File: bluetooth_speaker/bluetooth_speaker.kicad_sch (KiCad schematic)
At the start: 19 parts, among them J1 Conn_Coaxial, J2 USB_C_Receptacle_USB2.0_16P, J3 282836-4, U4 ESP32-D0WD-V3, Y1 40MHz(±10 ppm)

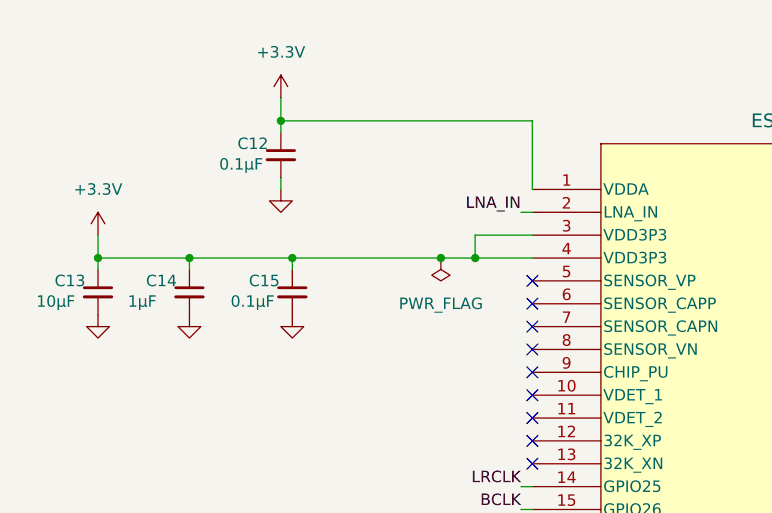
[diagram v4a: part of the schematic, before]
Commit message: Added missing inductor
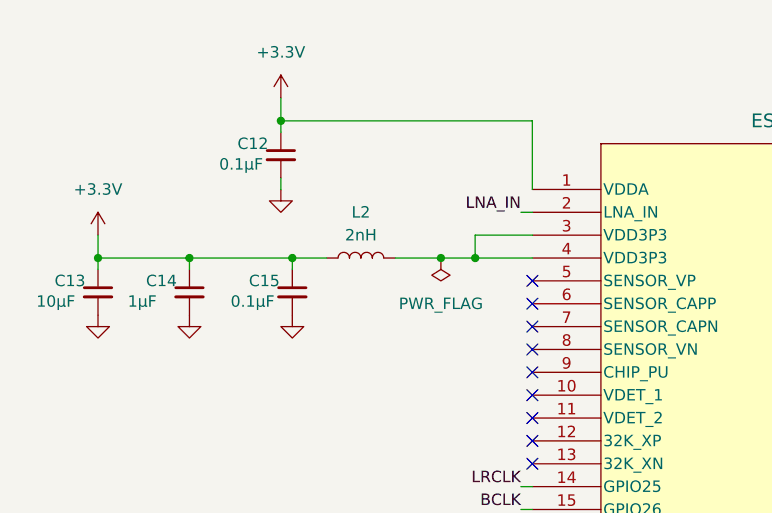
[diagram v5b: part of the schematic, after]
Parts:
- added L2: 2nH, SamacSys_Parts:MHQ1005, symbol Device:L
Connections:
- net +3.3V: now also L2.1; no longer U4.3 (VDD3P3), U4.4 (VDD3P3)
- new net: L2.2, U4.3 (VDD3P3), U4.4 (VDD3P3)
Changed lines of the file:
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@@
 	)
 	(junction
+		(at 43.18 39.37)
+		(diameter 0)
+		(color 0 0 0 0)
+	)
+	(junction
 		(at 63.5 39.37)
 		(diameter 0)
@@
 	)
 	(junction
+		(at 59.69 39.37)
+		(diameter 0)
+		(color 0 0 0 0)
+	)
+	(junction
 		(at 160.02 39.37)
 		(diameter 0)
@@
 	)
 	(junction
-		(at 59.69 39.37)
-		(diameter 0)
-		(color 0 0 0 0)
-	)
-	(junction
 		(at 168.91 127)
 		(diameter 0)
@@
 	)
 	(junction
-		(at 43.18 39.37)
-		(diameter 0)
-		(color 0 0 0 0)
-	)
-	(junction
 		(at 21.59 39.37)
 		(diameter 0)
@@
 	(wire
 		(pts
+			(xy 54.61 39.37) (xy 59.69 39.37)
+		)
+		(stroke
+			(width 0)
+			(type default)
+		)
+	)
+	(wire
+		(pts
 			(xy 236.22 133.35) (xy 242.57 133.35)
 		)
@@
 	(wire
 		(pts
+			(xy 43.18 39.37) (xy 46.99 39.37)
+		)
+		(stroke
+			(width 0)
+			(type default)
+		)
+	)
+	(wire
+		(pts
 			(xy 232.41 73.66) (xy 237.49 73.66)
 		)
@@
 	(wire
 		(pts
-			(xy 43.18 39.37) (xy 59.69 39.37)
-		)
-		(stroke
-			(width 0)
-			(type default)
-		)
-	)
-	(wire
-		(pts
 			(xy 21.59 39.37) (xy 31.75 39.37)
 		)
@@
 			)
 		)
-		(property "Datasheet" "~"
+		(property "Datasheet" "https://www.mouser.pl/ProductDetail/Taoglas/EMPCB.SMAFSTJ.C.HT?qs=AL7xPqYNrmS49k5WLHoXWA%3D%3D"
 			(at 250.19 133.35 0)
 			(effects
@@
 					(unit 1)
 				)
+			)
+		)
+	)
+	(symbol
+		(lib_id "Device:L")
+		(at 50.8 39.37 90)
+		(unit 1)
+		(exclude_from_sim no)
+		(in_bom yes)
+		(on_board yes)
+		(dnp no)
+		(fields_autoplaced yes)
+		(property "Reference" "L2"
+			(at 50.8 34.29 90)
+			(effects
+				(font
+					(size 1.27 1.27)
+				)
+			)
+		)
+		(property "Value" "2nH"
+			(at 50.8 36.83 90)
+			(effects
+				(font
+					(size 1.27 1.27)
+				)
+			)
+		)
+		(property "Footprint" "SamacSys_Parts:MHQ1005"
+			(at 50.8 39.37 0)
+			(effects
+				(font
+					(size 1.27 1.27)
+				)
+				(hide yes)
+			)
+		)
+		(property "Datasheet" "https://www.mouser.pl/ProductDetail/TDK/MHQ1005P2N0BTD25?qs=sGAEpiMZZMv126LJFLh8y5lwrxezZJ61ff3nV176I9k%3D"
+			(at 50.8 39.37 0)
+			(effects
+				(font
+					(size 1.27 1.27)
+				)
+				(hide yes)
+			)
+		)
+		(property "Description" "Inductor"
+			(at 50.8 39.37 0)
+			(effects
+				(font
+					(size 1.27 1.27)
+				)
+				(hide yes)
+			)
+		)
+		(pin "1"
+		)
+		(pin "2"
+		)
+		(instances
+			(project ""
+				(path "/13ff5fb5-140a-4554-92d9-4ae3849ea082"
+					(reference "L2")
+					(unit 1)
+				)

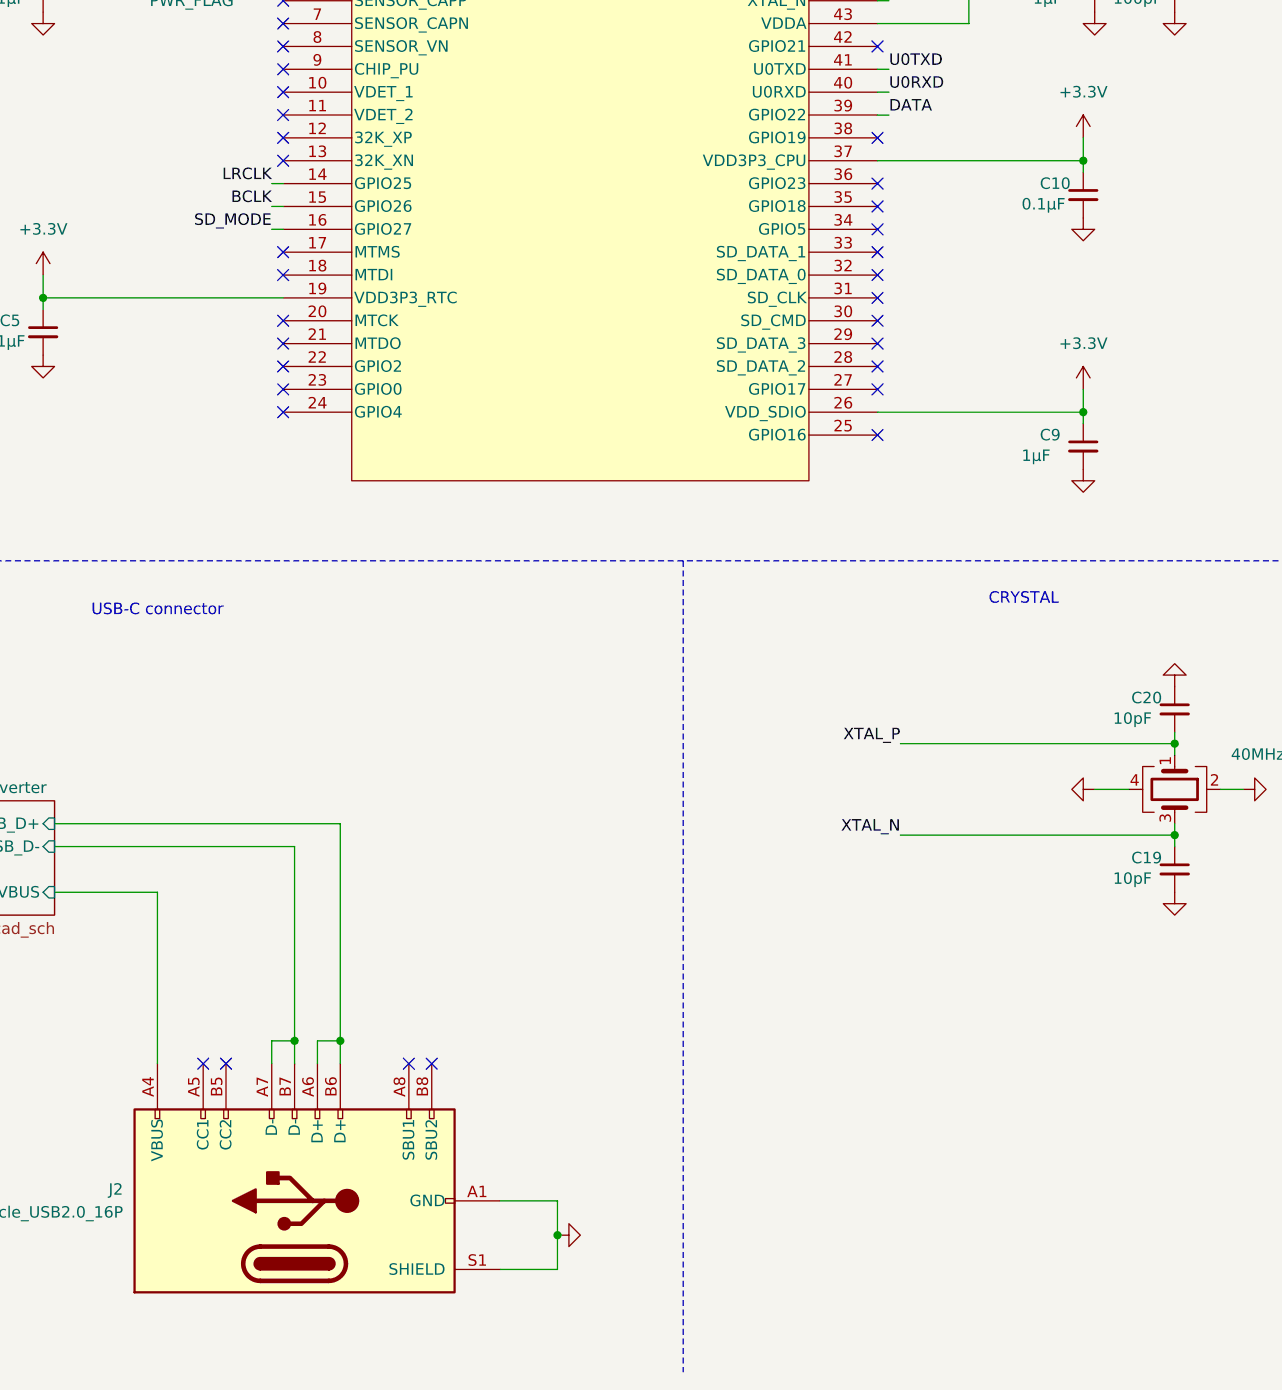
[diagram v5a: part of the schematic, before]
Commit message: Realigned components on PCB
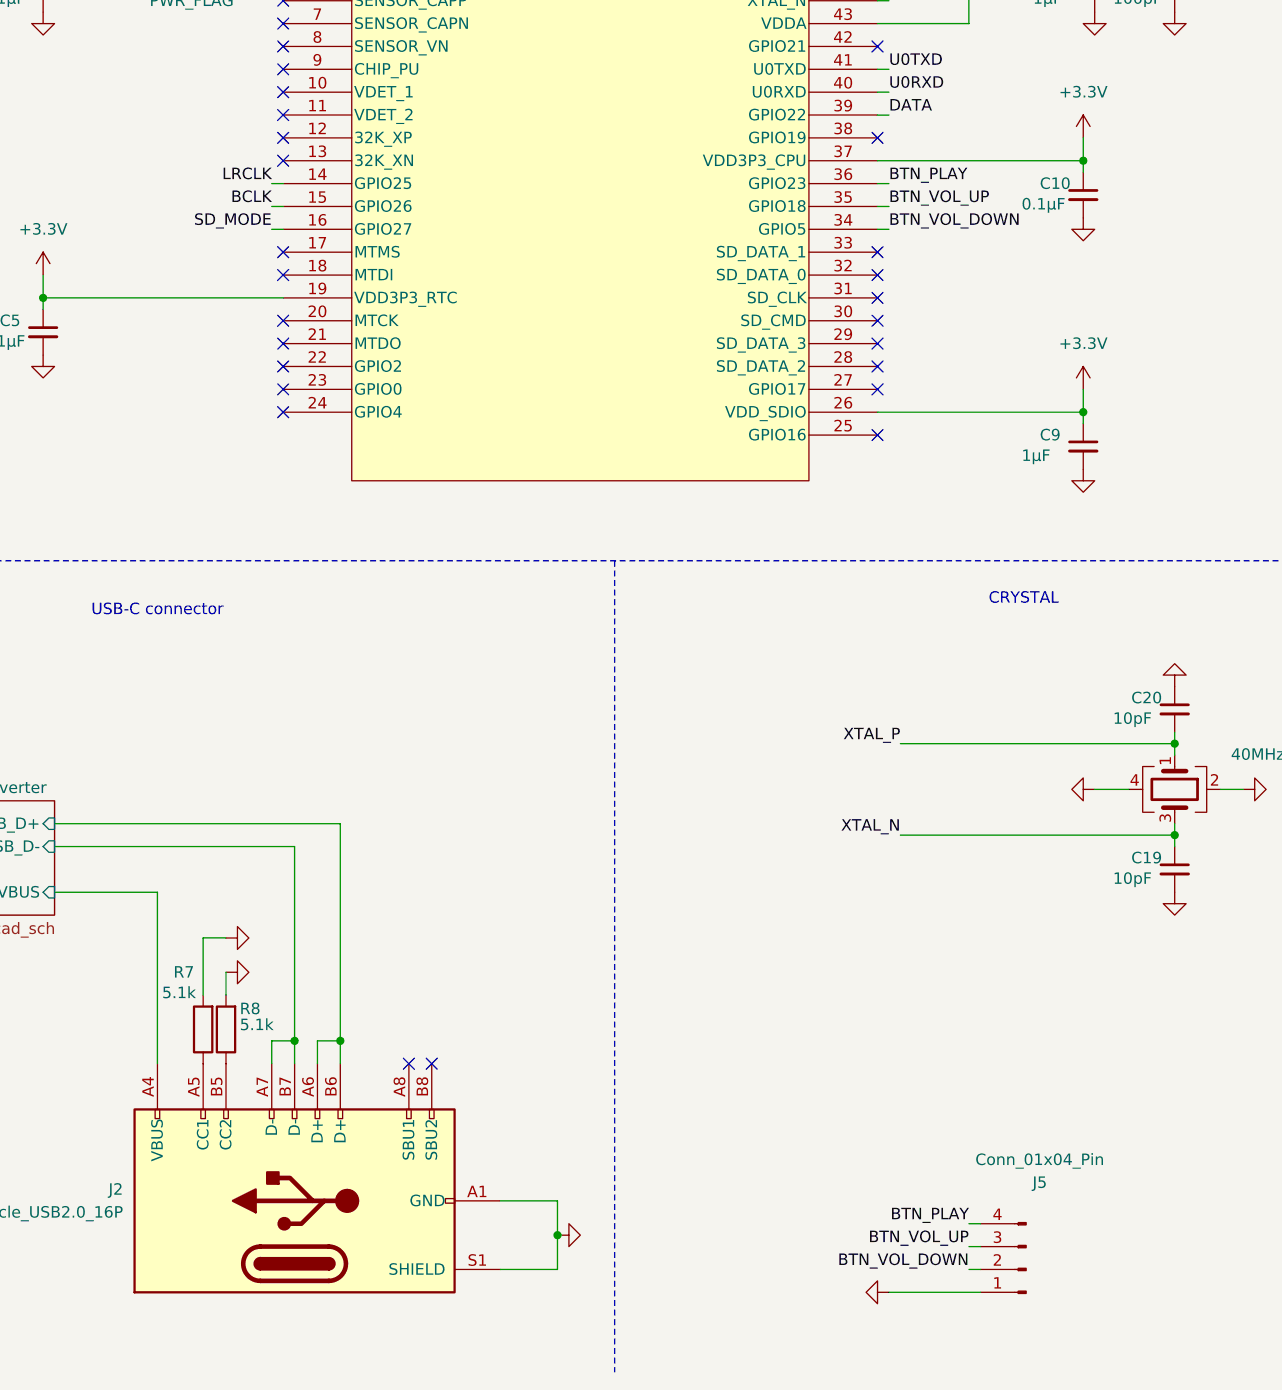
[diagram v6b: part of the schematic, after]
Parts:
- added J5: Conn_01x04_Pin, Connector_JST:JST_PH_B4B-PH-K_1x04_P2.00mm_Vertical, symbol Connector:Conn_01x04_Pin
- added R7, R8: 5.1k, Resistor_SMD:R_0603_1608Metric_Pad0.98x0.95mm_HandSolder, symbol Device:R
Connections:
- net GND: now also J5.1 (Pin_1), R7.2, R8.2
- net at J2.A5 (CC1): now also R7.1
- net at J2.B5 (CC2): now also R8.1
- net BTN_VOL_DOWN: now reaches U4.34 (GPIO5)
- net BTN_VOL_DOWN: now also J5.2 (Pin_2)
- net BTN_VOL_UP: now reaches U4.35 (GPIO18)
- net BTN_VOL_UP: now also J5.3 (Pin_3)
- net BTN_PLAY: now reaches U4.36 (GPIO23)
- net BTN_PLAY: now also J5.4 (Pin_4)
- no-connect marks 35 -> 30

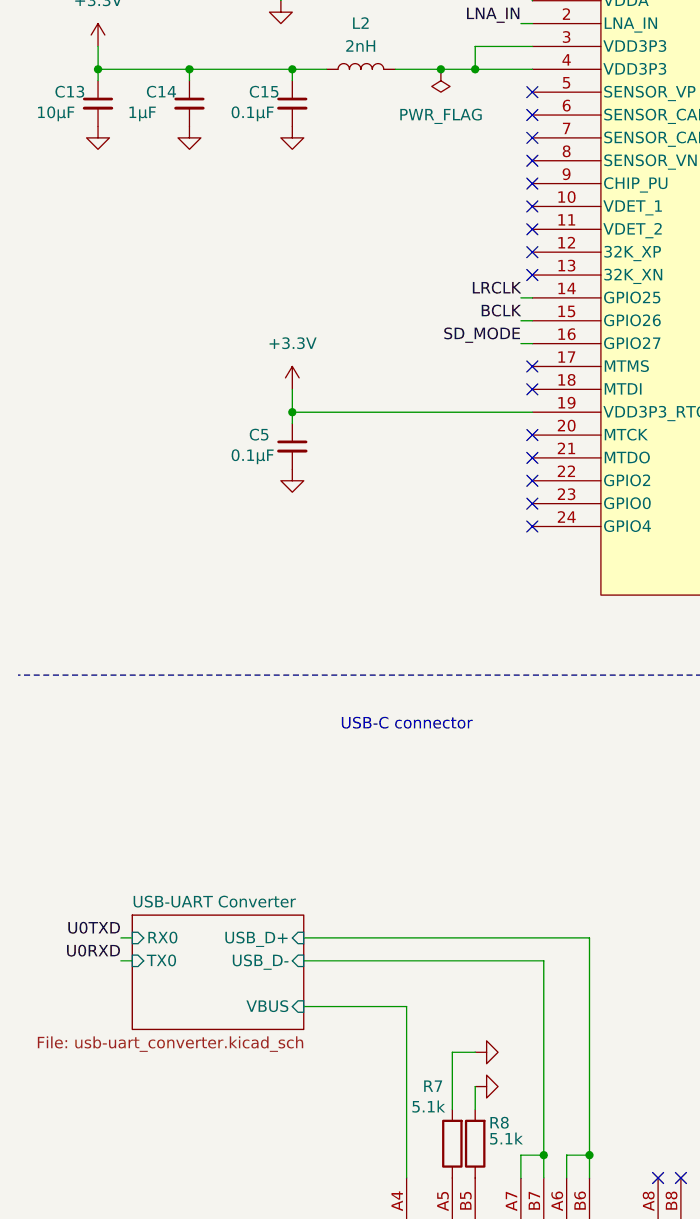
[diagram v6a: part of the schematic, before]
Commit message: Added auto-programming through CP2102
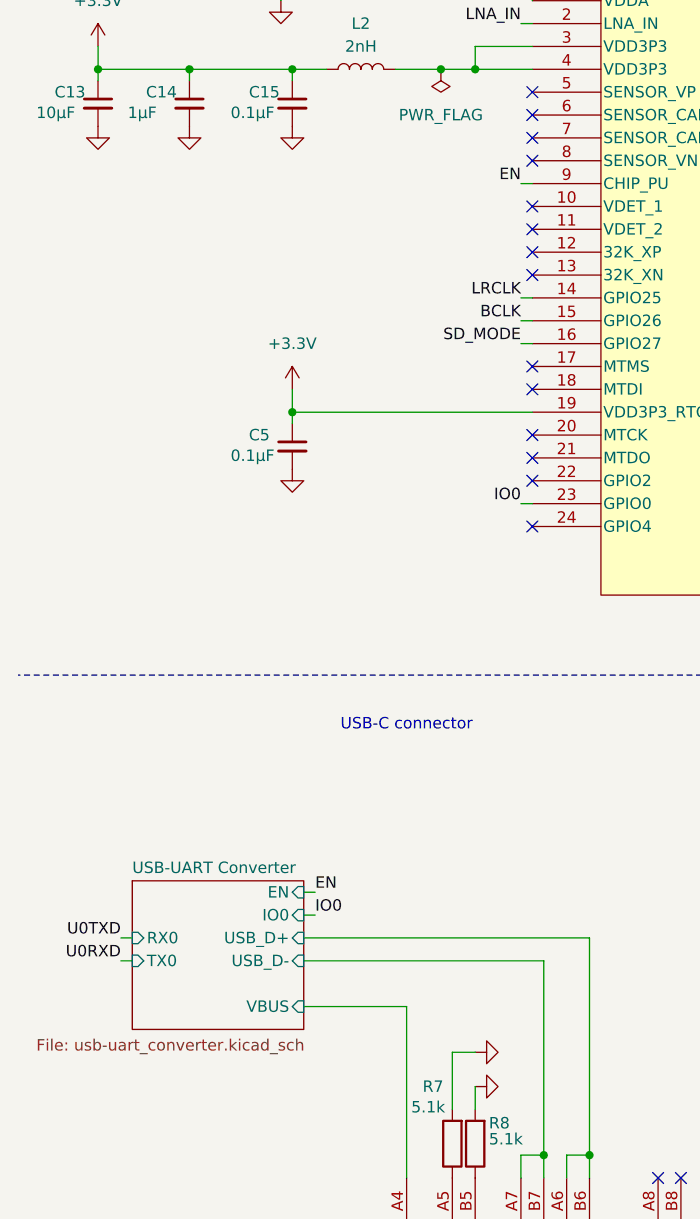
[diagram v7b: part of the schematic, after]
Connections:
- net IO0: now reaches U4.23 (GPIO0)
- net EN: now reaches U4.9 (CHIP_PU)
- no-connect marks 30 -> 28
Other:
- sheet USB-UART Converter ports: added EN, IO0; removed none
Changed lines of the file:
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@@
 	)
 	(no_connect
-		(at 69.85 52.07)
-	)
-	(no_connect
 		(at 135.89 80.01)
 	)
@@
 	)
 	(no_connect
-		(at 69.85 87.63)
-	)
-	(no_connect
 		(at 69.85 57.15)
 	)
@@
 	(wire
 		(pts
+			(xy 68.58 52.07) (xy 69.85 52.07)
+		)
+		(stroke
+			(width 0)
+			(type default)
+		)
+	)
+	(wire
+		(pts
 			(xy 41.91 24.13) (xy 69.85 24.13)
 		)
@@
 	(wire
 		(pts
+			(xy 44.45 133.35) (xy 45.72 133.35)
+		)
+		(stroke
+			(width 0)
+			(type default)
+		)
+	)
+	(wire
+		(pts
 			(xy 76.2 162.56) (xy 76.2 160.02)
 		)
@@
 	(wire
 		(pts
+			(xy 68.58 87.63) (xy 69.85 87.63)
+		)
+		(stroke
+			(width 0)
+			(type default)
+		)
+	)
+	(wire
+		(pts
 			(xy 228.6 133.35) (xy 222.25 133.35)
 		)
@@
 	(wire
 		(pts
+			(xy 44.45 130.81) (xy 45.72 130.81)
+		)
+		(stroke
+			(width 0)
+			(type default)
+		)
+	)
+	(wire
+		(pts
 			(xy 242.57 134.62) (xy 242.57 133.35)
 		)
@@
 		)
 	)
+	(label "EN"
+		(at 68.58 52.07 180)
+		(effects
+			(font
+				(size 1.27 1.27)
+			)
+			(justify right bottom)
+		)
+	)
 	(label "LRCLK"
 		(at 237.49 73.66 0)
@@
 		)
 	)
+	(label "IO0"
+		(at 45.72 133.35 0)
+		(effects
+			(font
+				(size 1.27 1.27)
+			)
+			(justify left bottom)
+		)
+	)
 	(label "SD_MODE"
 		(at 237.49 77.47 0)
@@
 		)
 	)
+	(label "EN"
+		(at 45.72 130.81 0)
+		(effects
+			(font
+				(size 1.27 1.27)
+			)
+			(justify left bottom)
+		)
+	)
+	(label "IO0"
+		(at 68.58 87.63 180)
+		(effects
+			(font
+				(size 1.27 1.27)
+			)
+			(justify right bottom)
+		)
+	)
 	(label "LRCLK"
 		(at 68.58 64.77 180)
@@
 	)
 	(sheet
-		(at 25.4 133.35)
-		(size 19.05 12.7)
+		(at 25.4 129.54)
+		(size 19.05 16.51)
 		(exclude_from_sim no)
 		(in_bom yes)
@@
 		)
 		(property "Sheetname" "USB-UART Converter"
-			(at 25.4 132.6384 0)
+			(at 25.4 128.8284 0)
 			(effects
 				(font
@@
 		)
 		(property "Sheetfile" "usb-uart_converter.kicad_sch"
-			(at 14.732 146.812 0)
+			(at 14.732 147.066 0)
 			(effects
 				(font
@@
 			(effects
 				(font
+					(size 1.27 1.27)
+				)
+				(justify right)
+			)
+		)
+		(pin "EN" input
+			(at 44.45 130.81 0)
+			(effects
+				(font
+					(size 1.27 1.27)
+				)
+				(justify right)
+			)
+		)
+		(pin "IO0" input
+			(at 44.45 133.35 0)
+			(effects
+				(font

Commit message: again
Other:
- moved on the sheet: J5
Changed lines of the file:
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@@
 	(wire
 		(pts
-			(xy 137.16 187.96) (xy 147.32 187.96)
+			(xy 135.89 185.42) (xy 146.05 185.42)
 		)
 		(stroke
@@
 	(wire
 		(pts
-			(xy 146.05 185.42) (xy 147.32 185.42)
+			(xy 144.78 182.88) (xy 146.05 182.88)
 		)
 		(stroke
@@
 	(wire
 		(pts
-			(xy 146.05 182.88) (xy 147.32 182.88)
+			(xy 144.78 180.34) (xy 146.05 180.34)
 		)
 		(stroke
@@
 	(wire
 		(pts
-			(xy 146.05 180.34) (xy 147.32 180.34)
+			(xy 144.78 177.8) (xy 146.05 177.8)
 		)
 		(stroke
@@
 	)
 	(label "BTN_VOL_UP"
-		(at 146.05 182.88 180)
+		(at 144.78 180.34 180)
 		(effects
 			(font
@@
 	)
 	(label "BTN_PLAY"
-		(at 146.05 180.34 180)
+		(at 144.78 177.8 180)
 		(effects
 			(font
@@
 	)
 	(label "BTN_VOL_DOWN"
-		(at 146.05 185.42 180)
+		(at 144.78 182.88 180)
 		(effects
 			(font
@@
 	(symbol
 		(lib_id "power:GND")
-		(at 137.16 187.96 270)
+		(at 135.89 185.42 270)
 		(unit 1)
 		(exclude_from_sim no)
@@
 		(fields_autoplaced yes)
 		(property "Reference" "#PWR047"
-			(at 130.81 187.96 0)
+			(at 129.54 185.42 0)
 			(effects
 				(font
@@
 		)
 		(property "Value" "GND"
-			(at 132.08 187.96 0)
+			(at 130.81 185.42 0)
 			(effects
 				(font
@@
 		)
 		(property "Footprint" ""
-			(at 137.16 187.96 0)
+			(at 135.89 185.42 0)
 			(effects
 				(font
@@
 		)
 		(property "Datasheet" ""
-			(at 137.16 187.96 0)
+			(at 135.89 185.42 0)
 			(effects
 				(font
@@
 		)
 		(property "Description" "Power symbol creates a global label with name \"GND\" , ground"
-			(at 137.16 187.96 0)
+			(at 135.89 185.42 0)
 			(effects
 				(font
@@
 	(symbol
 		(lib_id "Connector:Conn_01x04_Pin")
-		(at 152.4 185.42 180)
+		(at 151.13 182.88 180)
 		(unit 1)
 		(exclude_from_sim no)
@@
 		(dnp no)
 		(property "Reference" "J5"
-			(at 153.924 175.768 0)
+			(at 152.654 173.228 0)
 			(effects
 				(font
@@
 		)
 		(property "Value" "Conn_01x04_Pin"
-			(at 153.924 173.228 0)
+			(at 152.654 170.688 0)
 			(effects
 				(font
@@
 		)
 		(property "Footprint" "Connector_JST:JST_PH_B4B-PH-K_1x04_P2.00mm_Vertical"
-			(at 152.4 185.42 0)
+			(at 151.13 182.88 0)
 			(effects
 				(font
@@
 		)
 		(property "Datasheet" "~"
-			(at 152.4 185.42 0)
+			(at 151.13 182.88 0)
 			(effects
 				(font
@@
 		)
 		(property "Description" "Generic connector, single row, 01x04, script generated"
-			(at 152.4 185.42 0)
+			(at 151.13 182.88 0)
 			(effects
 				(font
